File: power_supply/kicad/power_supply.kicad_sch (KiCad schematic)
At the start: 6 parts, among them J1 pcie_98, U2 ESD5344D

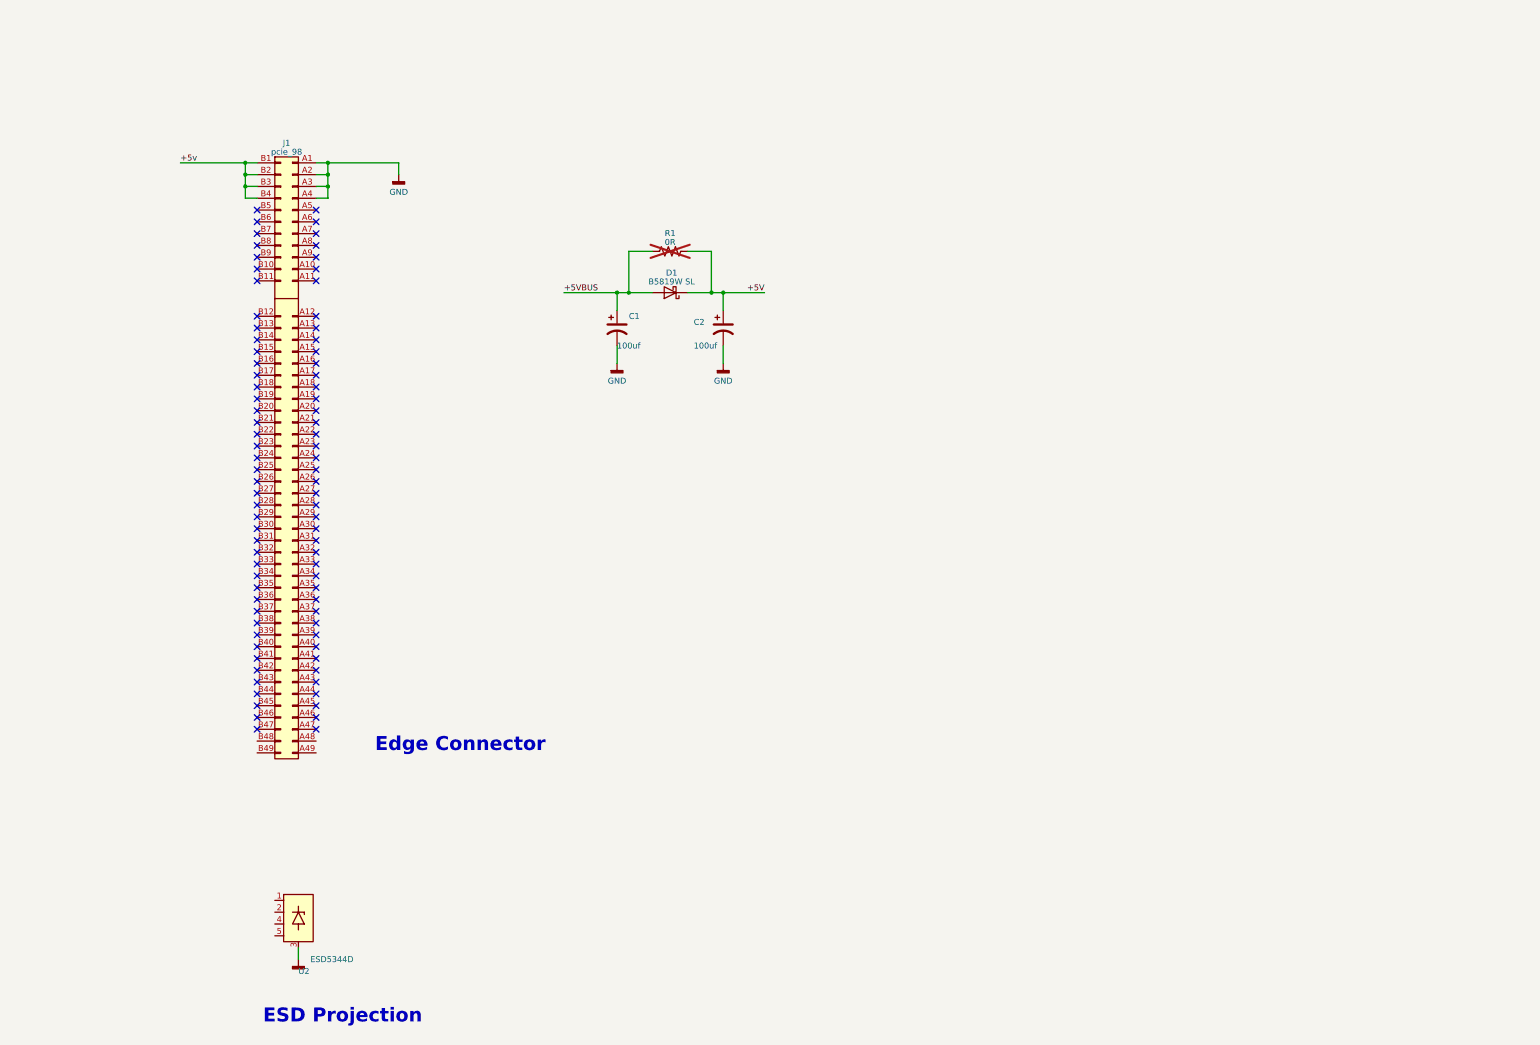
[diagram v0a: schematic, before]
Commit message: Set up a skeleton design of the pwoer supply.
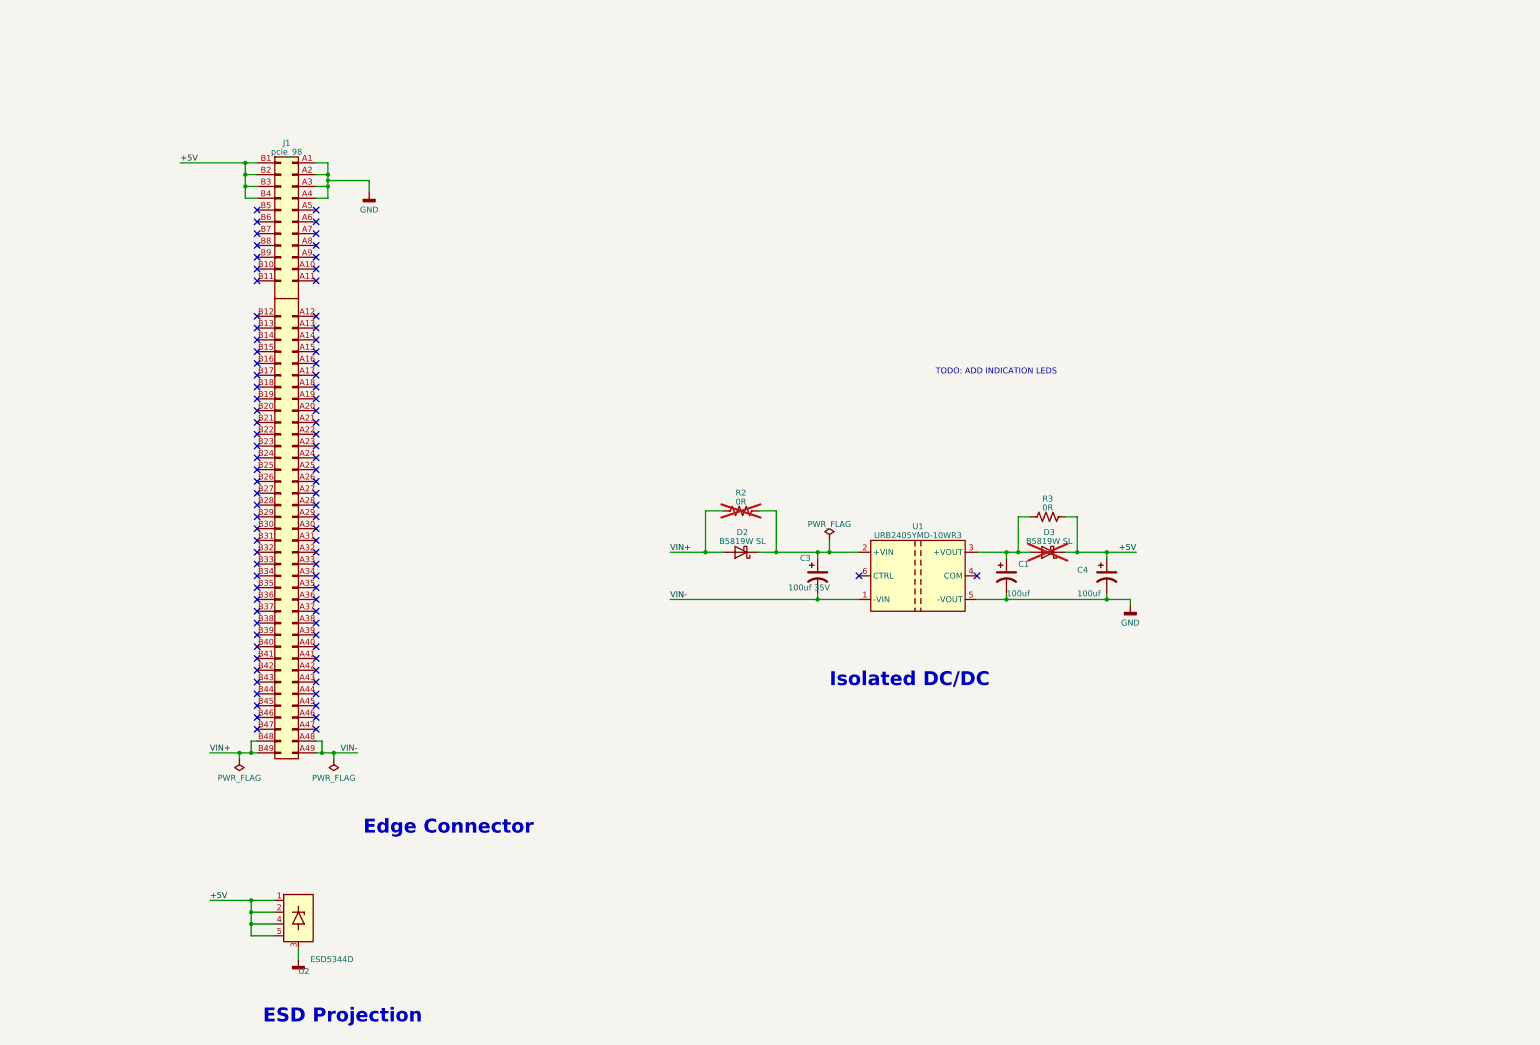
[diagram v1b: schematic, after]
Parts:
- removed C2: 100uf, power_supply:CP_Elec_5x5.4_JLCPCB, symbol Device:C_Polarized_US
- removed D1: B5819W SL, Diode_SMD:D_SOD-123, symbol Device:D_Schottky
- removed R1: 0R, Resistor_SMD:R_0805_2012Metric, symbol Device:R_US
- added C3: 100uf 35V, power_supply:CP_Elec_5x5.4_JLCPCB, symbol Device:C_Polarized_US
- added C4: 100uf, power_supply:CP_Elec_5x5.4_JLCPCB, symbol Device:C_Polarized_US
- added D2, D3: B5819W SL, Diode_SMD:D_SOD-123, symbol Device:D_Schottky
- added R2, R3: 0R, Resistor_SMD:R_0805_2012Metric, symbol Device:R_US
- added U1: URB2405YMD-10WR3, power_supply:DCDC, symbol power_supply:URB2405YMD-10WR3
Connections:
- net +5v is gone; now on net +5V: J1.B1 (Pin_b1), J1.B2 (Pin_b2), J1.B3 (Pin_b3), J1.B4 (Pin_b4)
- net +5V: now also U2.1 (D1), U2.2 (D2), U2.4 (D3), U2.5 (D4), C4.1, D3.1 (K), R3.2
- net GND: now also C4.2, U1.5 (-VOUT)
- net VIN-: now reaches J1.A48 (Pin_a48)
- net VIN-: now also J1.A49 (Pin_a49), C3.2, U1.1 (-VIN)
- net VIN+: now reaches J1.B48 (Pin_b48)
- net VIN+: now also J1.B49 (Pin_b49), D2.2 (A), R2.1
- net +5VBUS: no longer names the net of C1.1
- net +5VBUS: now also D3.2 (A), R3.1, U1.3 (+VOUT)
- new net: C3.1, D2.1 (K), R2.2, U1.2 (+VIN)
- no-connect marks 86 -> 88
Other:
- note added: "Isolated DC/DC"
- note added: "TODO: ADD INDICATION LEDS"
- moved on the sheet: C1

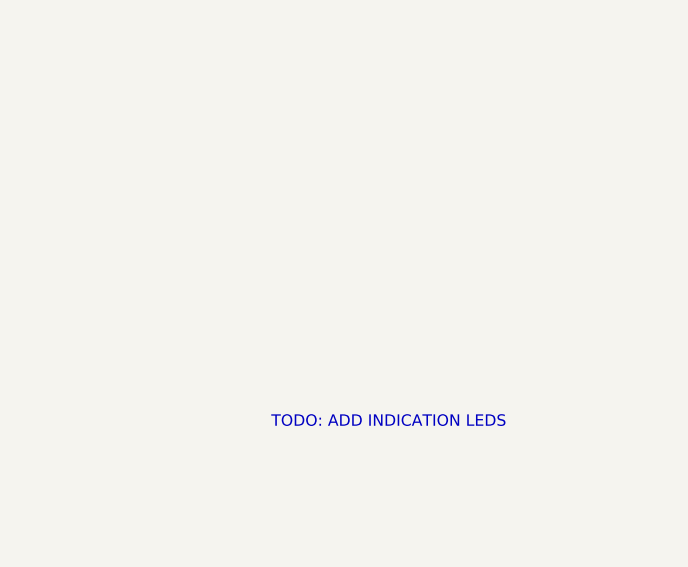
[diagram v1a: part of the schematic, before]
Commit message: Added TODO comments.
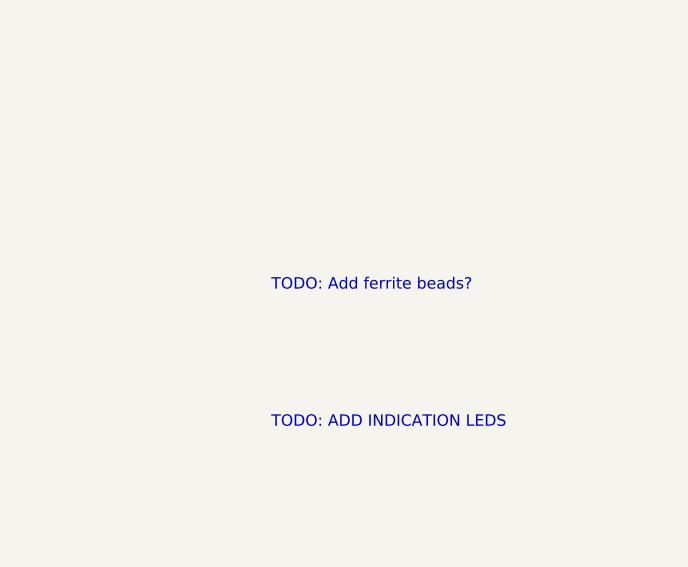
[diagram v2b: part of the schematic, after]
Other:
- note added: "TODO: Add ferrite beads?"
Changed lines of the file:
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@@
     (effects (font (size 3 3) (thickness 0.6) bold) (justify left bottom))
+  )
+  (text "TODO: Add ferrite beads?" (at 232.41 76.2 0)
+    (effects (font (size 1.27 1.27) (color 255 0 0 1)) (justify left bottom))
   )
   (text "Edge Connector" (at 109.22 190.5 0)

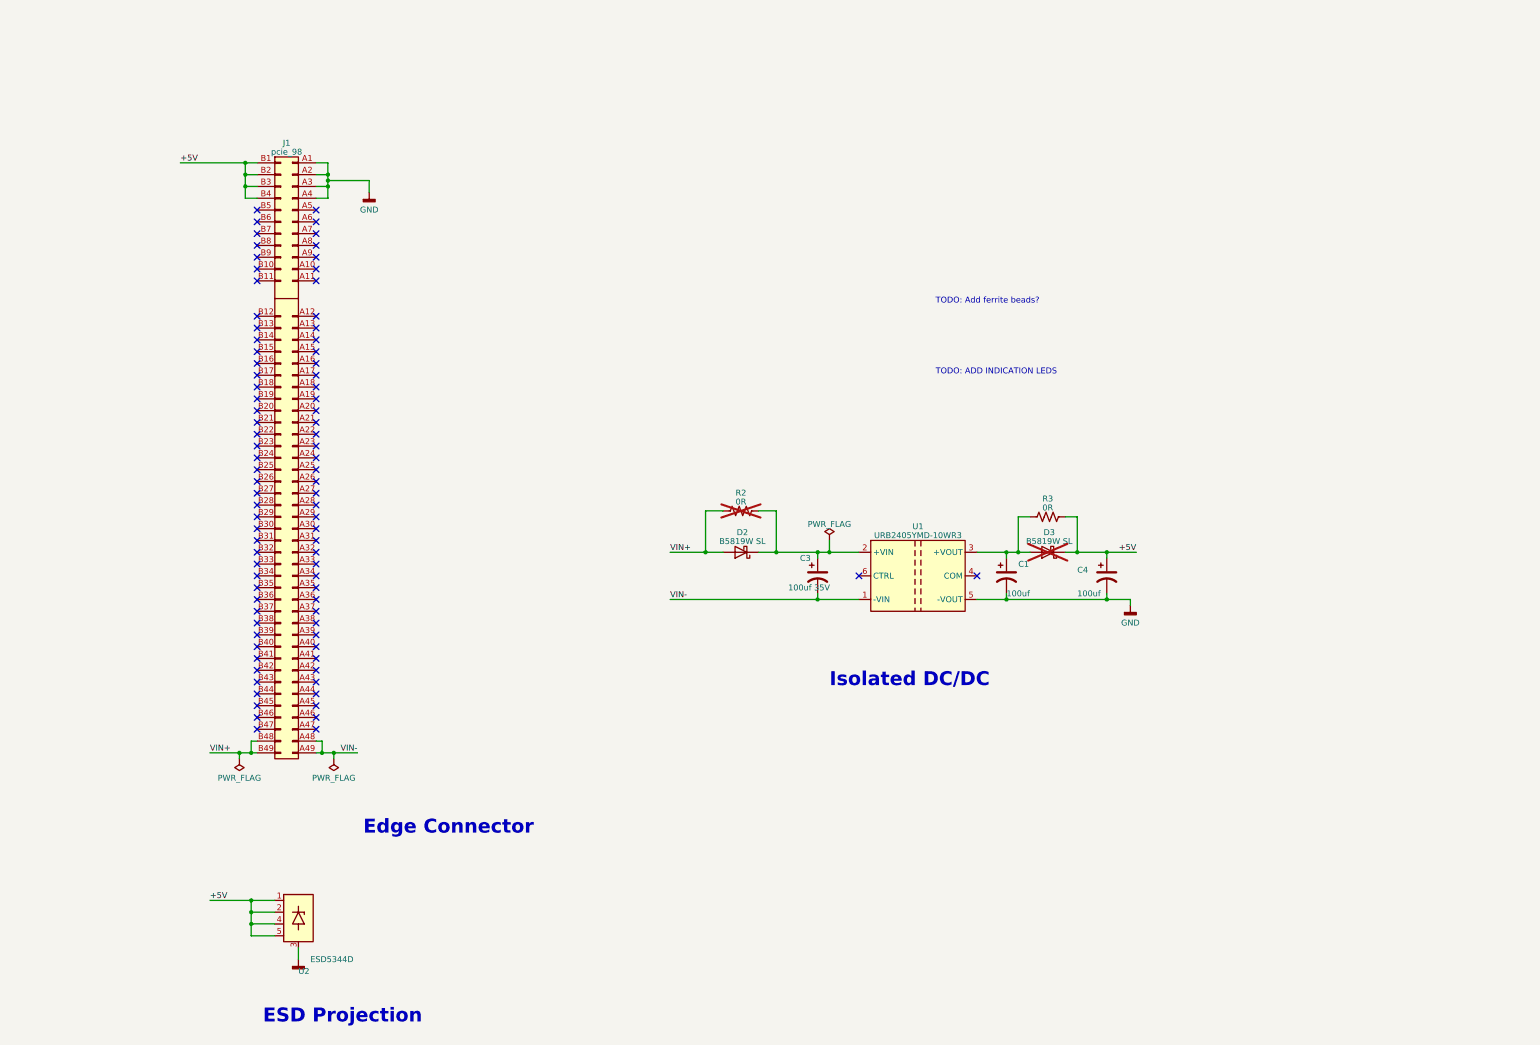
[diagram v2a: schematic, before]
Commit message: Added LEDs, test points, and LCSC ids.
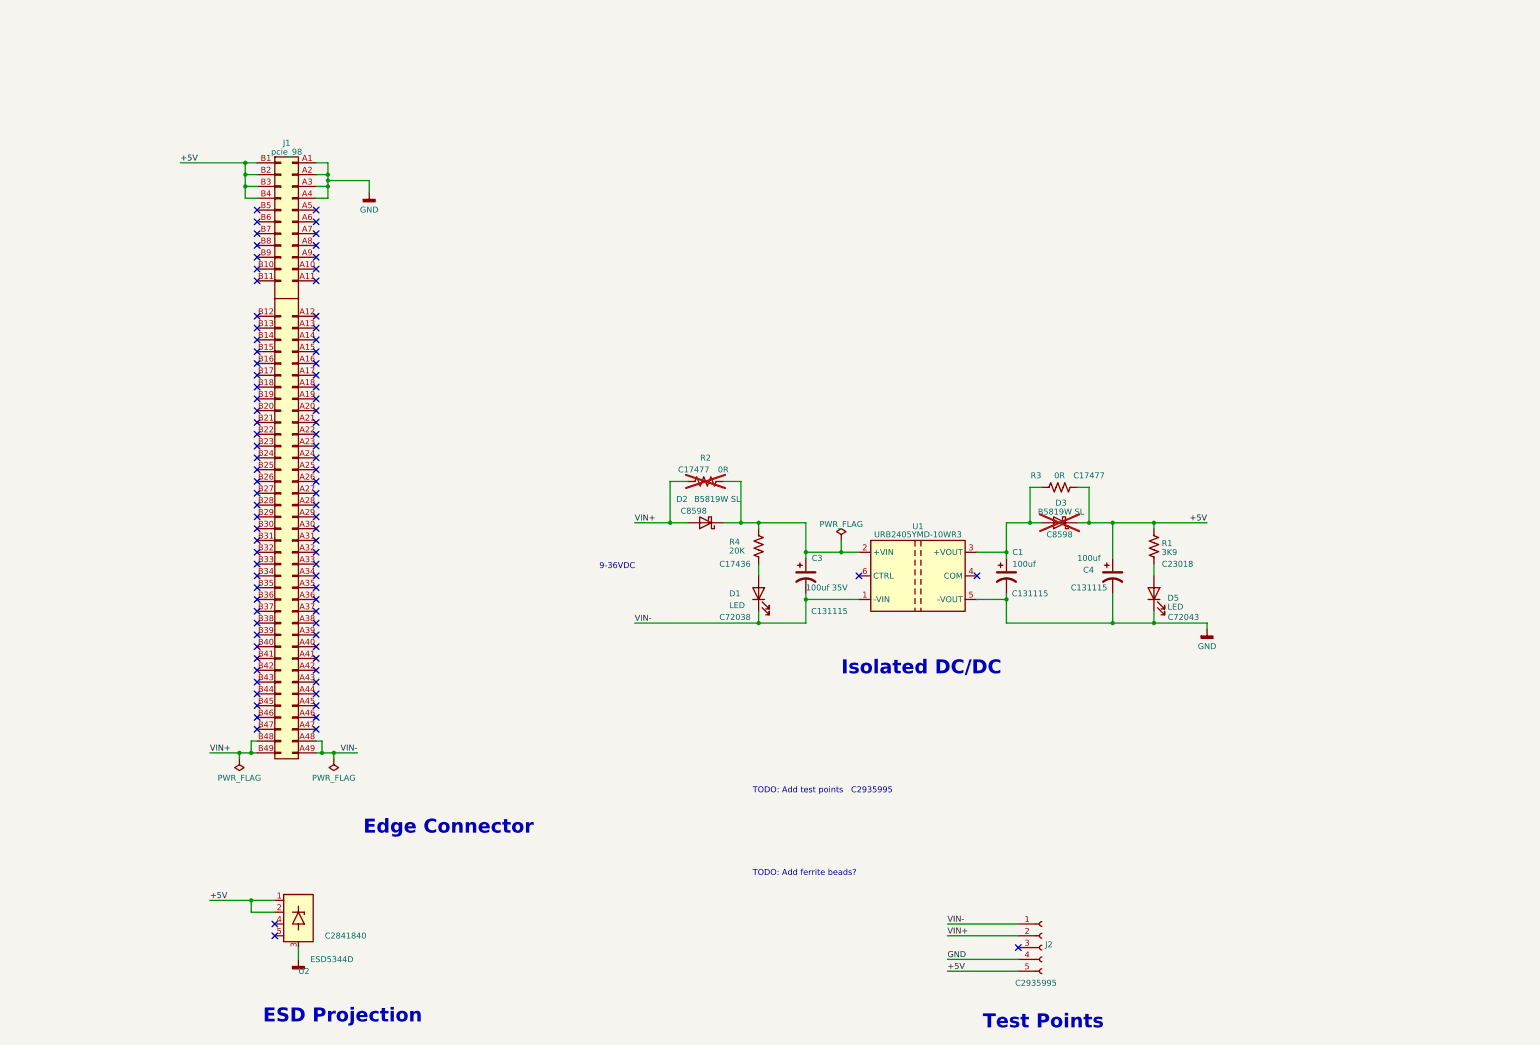
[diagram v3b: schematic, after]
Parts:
- added D1, D5: LED, LED_SMD:LED_0603_1608Metric, symbol Device:LED
- added J2: Conn_01x05_Socket, power_supply:PinSocket_1x05_P2.54mm_Horizontal, symbol Connector:Conn_01x05_Socket
- added R1: 3K9, Resistor_SMD:R_0603_1608Metric, symbol Device:R_US
- added R4: 20K, Resistor_SMD:R_0603_1608Metric, symbol Device:R_US
- U1: LCSC (none) -> C91825
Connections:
- net +5V: now also J2.5 (Pin_5), R1.1; no longer U2.4 (D3), U2.5 (D4)
- net GND: now also D5.1 (K), J2.4 (Pin_4)
- net VIN+: now also J2.2 (Pin_2)
- net VIN-: now also D1.1 (K), J2.1 (Pin_1)
- net at C3.1, D2.1 (K), R2.2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: now also R4.1
- new net: D5.2 (A), R1.2
- new net: D1.2 (A), R4.2
- no-connect marks 88 -> 91
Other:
- note added: "9-36VDC"
- note added: "TODO: Add test points C2935995"
- note added: "Test Points"
- note removed: "TODO: ADD INDICATION LEDS"
- moved on the sheet: C3, C4, D2, D3, R2, R3

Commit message: More cleanup of the power supply's PCB. Not done.
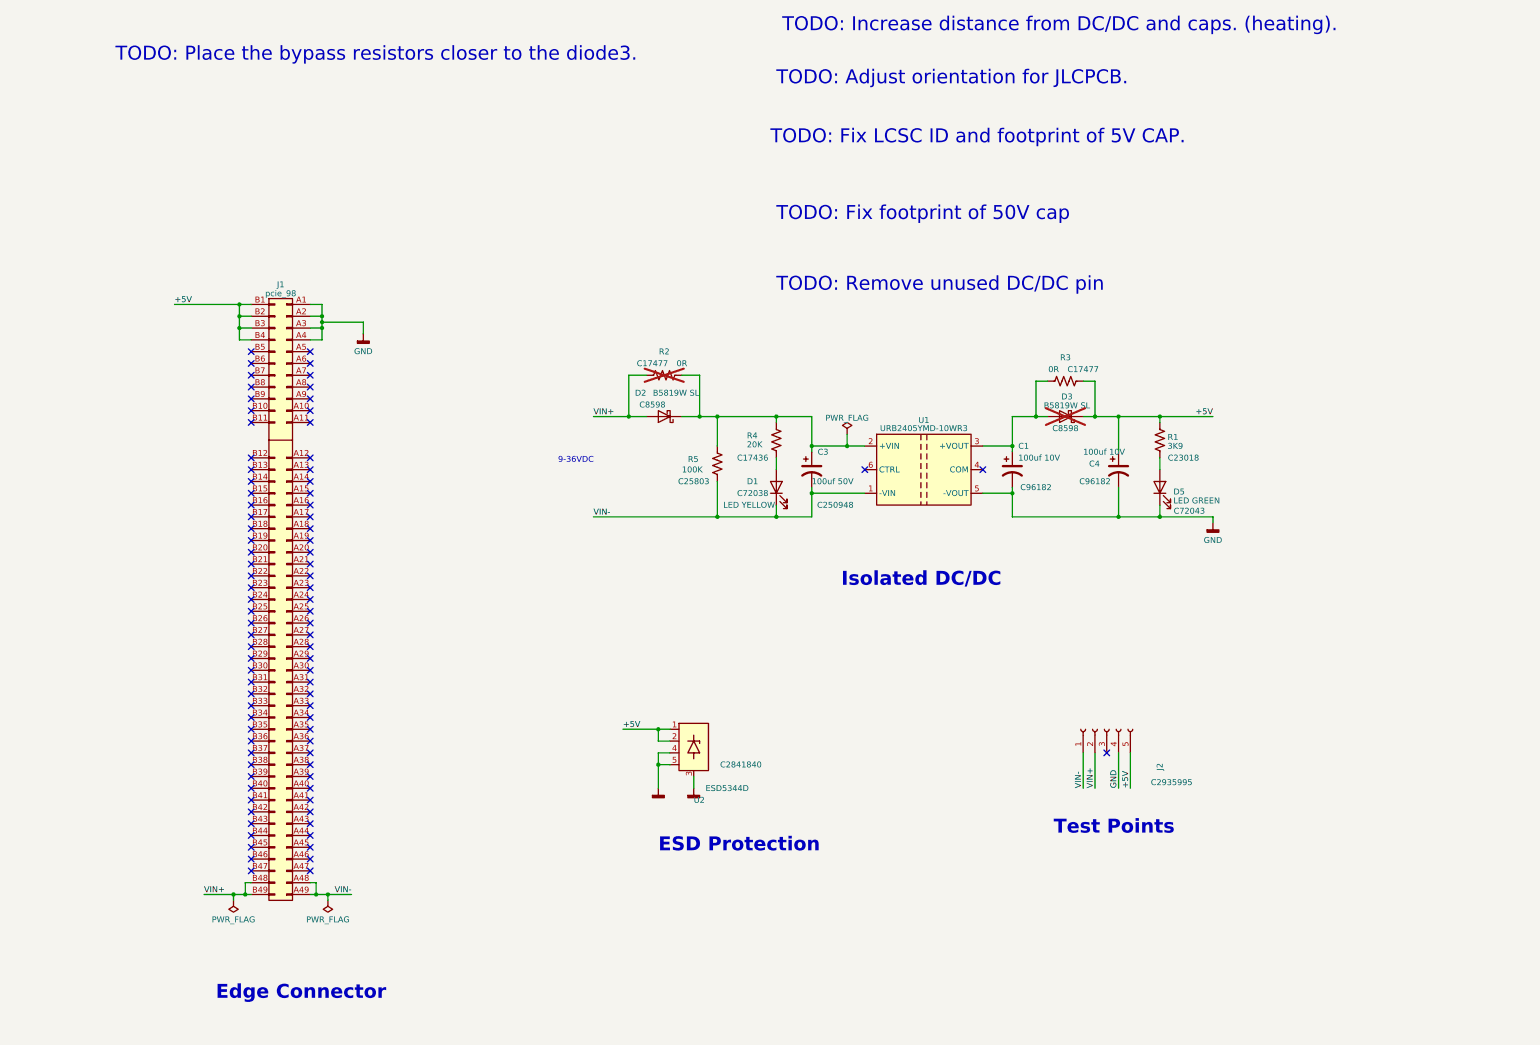
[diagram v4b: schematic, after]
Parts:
- added R5: 100K, Resistor_SMD:R_0603_1608Metric, symbol Device:R_US
- C1, C4: value 100uf -> 100uf 10V; LCSC C131115 -> C96182
- C3: value 100uf 35V -> 100uf 50V; footprint power_supply:CP_Elec_5x5.4_JLCPCB -> power_supply:C_Elec_8x10.2_JLCPCB; LCSC C131115 -> C250948
- D1: value LED -> LED YELLOW
- D5: value LED -> LED GREEN
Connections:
- net GND: now also U2.4 (D3), U2.5 (D4)
- net VIN-: now also R5.2
- net at C3.1, D2.1 (K), R2.2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: now also R5.1
- no-connect marks 91 -> 89
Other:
- note added: "ESD Protection"
- note added: "TODO: Adjust orientation for JLCPCB."
- note added: "TODO: Fix LCSC ID and footprint of 5V CAP."
- note added: "TODO: Fix footprint of 50V cap"
- note added: "TODO: Increase distance from DC/DC and caps. (heating)."
- note added: "TODO: Place the bypass resistors closer to the diode3."
- note added: "TODO: Remove unused DC/DC pin"
- note removed: "ESD Projection"
- note removed: "TODO: Add ferrite beads?"
- note removed: "TODO: Add test points C2935995"
- moved on the sheet: C1, C3, C4, D1, D2, D3, D5, J1, J2, R1, R2, R3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
